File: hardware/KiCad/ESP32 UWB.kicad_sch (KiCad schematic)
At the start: 55 parts, among them J1 HEADER-20P-2.54, J2 HEADER-12P-2.54, J3 10118194-0001LF, Q1 S8050, Q2 S8050, SW1 BUTTON, SW2 BUTTON, U1 AMS1117-3.3, U2 ESP32-C3-MINI-1-N4, U3 SILICON_LABS_CP2102N-A01-GQFN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, U4 DWM1000, U5 SK6812_3535

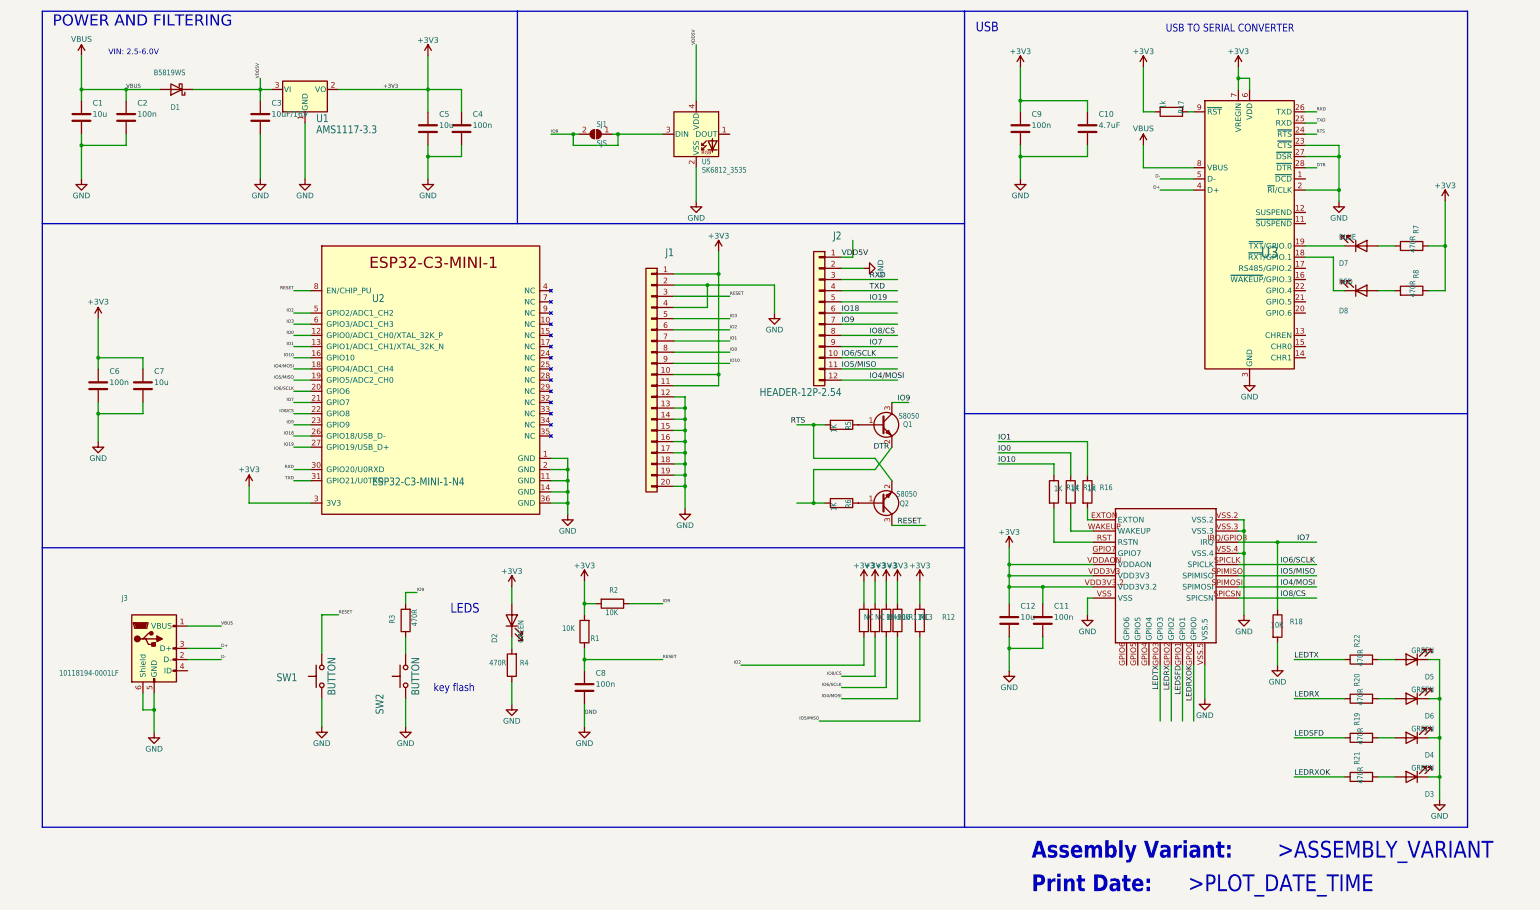
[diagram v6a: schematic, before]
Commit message: clean up schematic
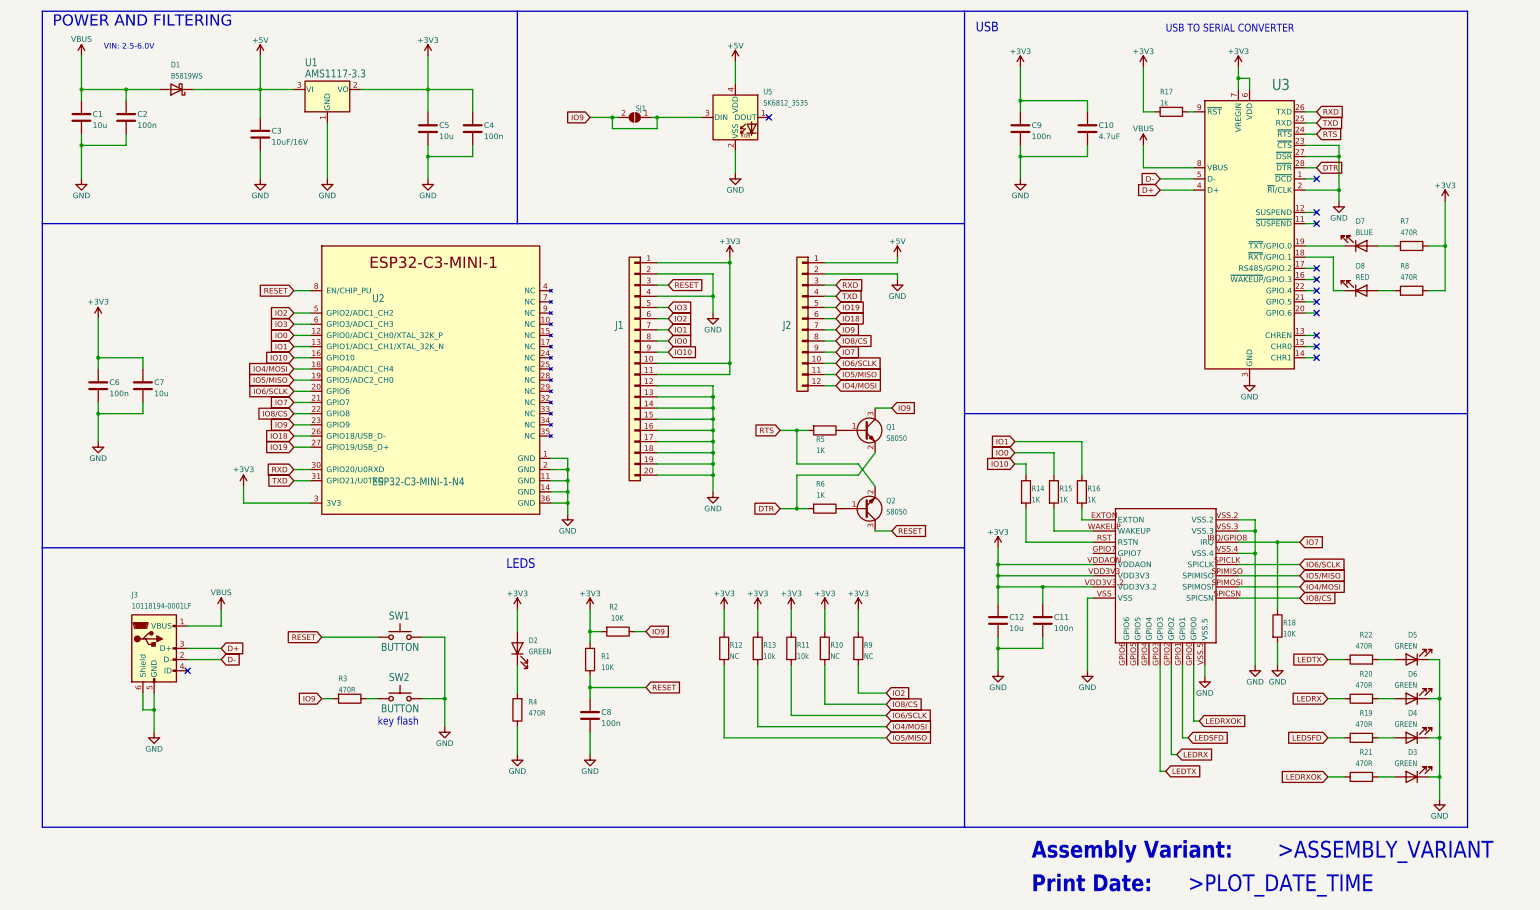
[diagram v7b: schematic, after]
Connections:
- net IO8/CS is gone; now on net IO8/CS: J2.8 (Pin_8), R10.2, U4.SPICSN
- net GND: now also SW1.2, SW2.2; no longer SW1.1, SW2.1
- net RESET: now also SW1.1; no longer SW1.2
- net at R3.1: now also SW2.1; no longer SW2.2
- net IO4/MOSI renamed IO4/MOSI
- net IO5/MISO renamed IO5/MISO
- net IO6/SCLK renamed IO6/SCLK
- net VDD5V renamed +5V
- no-connect marks 0 -> 13
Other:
- moved on the sheet: C12, C3, C4, C8, D2, J1, J2, Q1, Q2, R1, R10, R11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

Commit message: add keepout zone and labels for LEDs
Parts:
- D2: Meaning (none) -> PWR
- D3: Meaning (none) -> RXDK
- D4: Meaning (none) -> SFD
- D6, D8: Meaning (none) -> RX
- D7: Meaning (none) -> TX
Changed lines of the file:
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@@
+      (effects (font (size 1.27 1.27)) hide)
+    )
+    (property "Meaning" "RX" (id 4) (at 321.31 81.28 0)
       (effects (font (size 1.27 1.27)) hide)
     )
@@
   (symbol (lib_id "power:+5V") (at 71.12 27.94 0) (mirror y) (unit 1)
     (in_bom yes) (on_board yes)
-    (property "Reference" "#PWR?" (id 0) (at 71.12 31.75 0)
+    (property "Reference" "#PWR0145" (id 0) (at 71.12 31.75 0)
       (effects (font (size 1.27 1.27)) hide)
     )
@@
       (effects (font (size 1.27 1.27)) hide)
     )
+    (property "Meaning" "SFD" (id 4) (at 332.74 182.88 0)
+      (effects (font (size 1.27 1.27)) hide)
+    )
     (pin "1")
     (pin "2")
@@
   (symbol (lib_id "power:VBUS") (at 62.23 153.67 0) (unit 1)
     (in_bom yes) (on_board yes)
-    (property "Reference" "#PWR?" (id 0) (at 62.23 157.48 0)
+    (property "Reference" "#PWR0102" (id 0) (at 62.23 157.48 0)
       (effects (font (size 1.27 1.27)) hide)
     )
@@
       (effects (font (size 1.27 1.27)) hide)
     )
+    (property "Meaning" "RX" (id 4) (at 332.74 173.99 0)
+      (effects (font (size 1.27 1.27)) hide)
+    )
     (pin "1")
     (pin "2")
@@
   (symbol (lib_id "power:+5V") (at 215.9 73.66 0) (mirror y) (unit 1)
     (in_bom yes) (on_board yes)
-    (property "Reference" "#PWR?" (id 0) (at 215.9 77.47 0)
+    (property "Reference" "#PWR0143" (id 0) (at 215.9 77.47 0)
       (effects (font (size 1.27 1.27)) hide)
     )
@@
       (effects (font (size 1.27 1.27)) hide)
     )
+    (property "Meaning" "RXDK" (id 4) (at 332.74 191.77 0)
+      (effects (font (size 1.27 1.27)) hide)
+    )
     (pin "1")
     (pin "2")
@@
   (symbol (lib_id "power:+5V") (at 179.07 29.21 0) (mirror y) (unit 1)
     (in_bom yes) (on_board yes)
-    (property "Reference" "#PWR?" (id 0) (at 179.07 33.02 0)
+    (property "Reference" "#PWR0144" (id 0) (at 179.07 33.02 0)
       (effects (font (size 1.27 1.27)) hide)
     )
@@
       (effects (font (size 1.27 1.27)) hide)
     )
+    (property "Meaning" "PWR" (id 4) (at 129.54 162.56 90)
+      (effects (font (size 1.27 1.27)) hide)
+    )
     (pin "1")
     (pin "2")
@@
       (effects (font (size 1.27 1.27)) hide)
     )
+    (property "Meaning" "TX" (id 4) (at 321.31 71.12 0)
+      (effects (font (size 1.27 1.27)) hide)
+    )
     (pin "1")
     (pin "2")
@@
       (reference "#PWR0101") (unit 1) (value "+3V3") (footprint "")
     )
+    (path "/84ce102b-a7ba-4208-9116-a7b57fe5f272"
+      (reference "#PWR0102") (unit 1) (value "VBUS") (footprint "")
+    )
     (path "/97cc39d8-c871-4e37-a9ca-8f3a0ea043e7"
       (reference "#PWR0103") (unit 1) (value "GND") (footprint "")
@@
       (reference "#PWR0142") (unit 1) (value "GND") (footprint "")
     )
+    (path "/98491910-fd7f-4f40-b30e-2a357671c410"
+      (reference "#PWR0143") (unit 1) (value "+5V") (footprint "")
+    )
+    (path "/bbaff0f6-7bba-4fa4-b20d-82f0f61f1680"
+      (reference "#PWR0144") (unit 1) (value "+5V") (footprint "")
+    )
     (path "/1319c00b-2c1e-438c-8543-6b2a8902ed4b"
-      (reference "#PWR?") (unit 1) (value "+5V") (footprint "")
-    )
-    (path "/84ce102b-a7ba-4208-9116-a7b57fe5f272"
-      (reference "#PWR?") (unit 1) (value "VBUS") (footprint "")
-    )
-    (path "/98491910-fd7f-4f40-b30e-2a357671c410"
-      (reference "#PWR?") (unit 1) (value "+5V") (footprint "")
-    )
-    (path "/bbaff0f6-7bba-4fa4-b20d-82f0f61f1680"
-      (reference "#PWR?") (unit 1) (value "+5V") (footprint "")
+      (reference "#PWR0145") (unit 1) (value "+5V") (footprint "")
     )
     (path "/02b39166-9f7a-4094-8bda-785f43edf3d1"
